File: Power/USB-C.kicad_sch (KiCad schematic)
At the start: 40 parts, among them J1 USB_C_Receptacle_PowerOnly_6P, J2 Barrel_Jack_Switch, J3 Barrel_Jack_Switch, J4 Barrel_Jack_Switch, J5 Barrel_Jack_Switch, SW1 15v12, SW2 12v9, U1 HUSB237, U2 TPS73801, U3 TPS73801

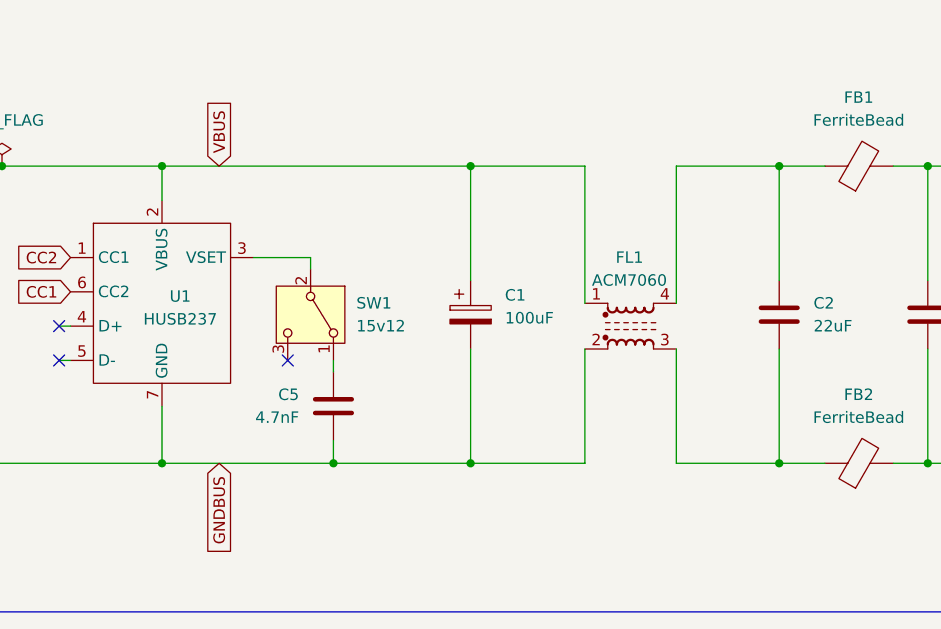
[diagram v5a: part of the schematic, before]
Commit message: Power board: move common mode choke to front
I don't do the nice 3D models, because I'm lazy and it's too much of a
hassle.  But it also means that it wasn't visually obvious that the
common mode choke ends up being very inconvenient on the back of the
board.

I'm perfectly fine with the usual low profile SMD components there, but
that choke is 3.5mm high, which is about twice as much as the other
components.

It's not that bad on the power board (which I don't have an enclosure
for anyway, although I'm looking at maybe just encasing it in resin with
a mold).  On the VGND effects board it's a non-starter.

Of course, I'm not convinced the choke actually matters, and the answer
may just be to remove it again, but until I see the effects of it let's
just move it to the front of the board.

It's going to be inconvenient to solder - I much prefer the hotplate -
but particularly on the power board I already have that USB-C connector
that I do with a hot-air station, and they are right next to each other,
so I can probably just do them together.

I'll have to think about the effects board more.  I don't actually have
room on the top of the board because I want to keep the electrolytics up
there, and keep the area in the middle clear for if I ever re-introduce
the joiner/splitter model with a third audio jack.

I think the inter-board connector there in the middle was a mistake.
It's in the way not only for this choke, but for any single-pot design
if I ever do one.

So the solution may be that I'll just have to move the connector around,
but that obviously means that I lose backwards compatibility with
existing effects boards.  Not really a big deal - unlike the enclosure
changes, it's easy enough to just do new boards - but if I make that
kind of change I want to make sure I think it through and get it right.

So let's wait to see if the choke even makes a difference.

Signed-off-by: Linus Torvalds <torvalds@linux-foundation.org>
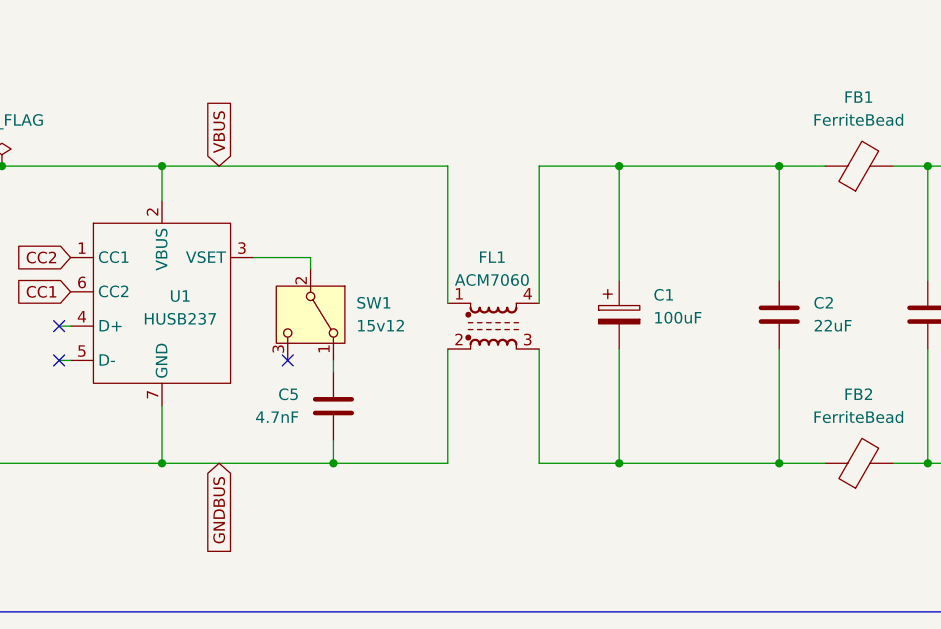
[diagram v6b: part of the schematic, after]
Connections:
- net GNDBUS: no longer C1.2
- net VBUS: no longer C1.1
- net at C2.1, FB1.1, FL1.4: now also C1.1
- net at C2.2, FB2.1, FL1.3: now also C1.2
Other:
- moved on the sheet: C1, FL1
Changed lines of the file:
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@@
 	)
 	(junction
-		(at 27.94 146.05)
+		(at 129.54 50.8)
 		(diameter 0)
 		(color 0 0 0 0)
 	)
 	(junction
-		(at 44.45 130.81)
+		(at 129.54 83.82)
 		(diameter 0)
 		(color 0 0 0 0)
 	)
 	(junction
-		(at 100.33 140.97)
+		(at 27.94 146.05)
 		(diameter 0)
 		(color 0 0 0 0)
 	)
 	(junction
-		(at 113.03 50.8)
+		(at 44.45 130.81)
 		(diameter 0)
 		(color 0 0 0 0)
 	)
 	(junction
-		(at 78.74 50.8)
+		(at 100.33 140.97)
 		(diameter 0)
 		(color 0 0 0 0)
 	)
 	(junction
-		(at 97.79 83.82)
+		(at 78.74 50.8)
 		(diameter 0)
 		(color 0 0 0 0)
 	)
 	(junction
-		(at 113.03 83.82)
+		(at 97.79 83.82)
 		(diameter 0)
 		(color 0 0 0 0)
@@
 	(wire
 		(pts
-			(xy 135.89 83.82) (xy 147.32 83.82)
+			(xy 120.65 83.82) (xy 129.54 83.82)
+		)
+		(stroke
+			(width 0)
+			(type default)
+		)
+	)
+	(wire
+		(pts
+			(xy 129.54 50.8) (xy 129.54 63.5)
 		)
 		(stroke
@@
 	(wire
 		(pts
-			(xy 135.89 50.8) (xy 147.32 50.8)
+			(xy 120.65 50.8) (xy 129.54 50.8)
 		)
 		(stroke
@@
 	(wire
 		(pts
-			(xy 113.03 50.8) (xy 113.03 63.5)
+			(xy 25.4 143.51) (xy 27.94 143.51)
 		)
 		(stroke
@@
 	(wire
 		(pts
-			(xy 25.4 143.51) (xy 27.94 143.51)
+			(xy 129.54 71.12) (xy 129.54 83.82)
 		)
 		(stroke
@@
 	(wire
 		(pts
-			(xy 113.03 83.82) (xy 125.73 83.82)
+			(xy 97.79 83.82) (xy 110.49 83.82)
 		)
 		(stroke
@@
 	(wire
 		(pts
-			(xy 135.89 71.12) (xy 135.89 83.82)
+			(xy 120.65 71.12) (xy 120.65 83.82)
 		)
 		(stroke
@@
 	(wire
 		(pts
-			(xy 113.03 71.12) (xy 113.03 83.82)
+			(xy 78.74 50.8) (xy 110.49 50.8)
 		)
 		(stroke
@@
 	(wire
 		(pts
-			(xy 113.03 50.8) (xy 125.73 50.8)
+			(xy 95.25 60.96) (xy 95.25 62.23)
 		)
 		(stroke
@@
 	(wire
 		(pts
-			(xy 95.25 60.96) (xy 95.25 62.23)
+			(xy 110.49 71.12) (xy 110.49 83.82)
 		)
 		(stroke
@@
 	(wire
 		(pts
-			(xy 125.73 71.12) (xy 125.73 83.82)
+			(xy 129.54 83.82) (xy 147.32 83.82)
 		)
 		(stroke
@@
 	(wire
 		(pts
-			(xy 78.74 50.8) (xy 113.03 50.8)
-		)
-		(stroke
-			(width 0)
-			(type default)
-		)
-	)
-	(wire
-		(pts
 			(xy 44.45 130.81) (xy 44.45 138.43)
 		)
@@
 	(wire
 		(pts
-			(xy 180.34 83.82) (xy 194.31 83.82)
+			(xy 129.54 50.8) (xy 147.32 50.8)
 		)
 		(stroke
@@
 	(wire
 		(pts
-			(xy 100.33 139.7) (xy 100.33 140.97)
+			(xy 180.34 83.82) (xy 194.31 83.82)
 		)
 		(stroke
@@
 	(wire
 		(pts
-			(xy 97.79 83.82) (xy 113.03 83.82)
+			(xy 100.33 139.7) (xy 100.33 140.97)
 		)
 		(stroke
@@
 	(wire
 		(pts
-			(xy 135.89 66.04) (xy 135.89 50.8)
+			(xy 120.65 66.04) (xy 120.65 50.8)
 		)
 		(stroke
@@
 	(wire
 		(pts
-			(xy 125.73 50.8) (xy 125.73 66.04)
+			(xy 110.49 50.8) (xy 110.49 66.04)
 		)
 		(stroke
@@
 	(symbol
 		(lib_id "Filter:Choke_CommonMode_FerriteCore_1423")
-		(at 130.81 68.58 0)
+		(at 115.57 68.58 0)
 		(unit 1)
 		(exclude_from_sim no)
@@
 		(fields_autoplaced yes)
 		(property "Reference" "FL1"
-			(at 130.683 60.96 0)
+			(at 115.443 60.96 0)
 			(effects
 				(font
@@
 		)
 		(property "Value" "ACM7060"
-			(at 130.683 63.5 0)
+			(at 115.443 63.5 0)
 			(effects
 				(font
@@
 		)
 		(property "Footprint" "Inductor_SMD:L_CommonModeChoke_TDK_ACM7060"
-			(at 130.81 74.93 0)
+			(at 115.57 74.93 0)
 			(effects
 				(font
@@
 		)
 		(property "Datasheet" "~"
-			(at 130.81 76.835 0)
+			(at 115.57 76.835 0)
 			(effects
 				(font
@@
 		)
 		(property "Description" "Generic common-mode choke, ferrite core, 1423 pin order"
-			(at 130.81 68.58 0)
+			(at 115.57 68.58 0)
 			(effects
 				(font
@@
 	(symbol
 		(lib_id "Device:C_Polarized")
-		(at 113.03 67.31 0)
+		(at 129.54 67.31 0)
 		(unit 1)
 		(exclude_from_sim no)
@@
 		(on_board yes)
 		(dnp no)
-		(fields_autoplaced yes)
 		(property "Reference" "C1"
-			(at 116.84 65.1509 0)
+			(at 133.35 65.1509 0)
 			(effects
 				(font
@@
 		)
 		(property "Value" "100uF"
-			(at 116.84 67.6909 0)
+			(at 133.35 67.6909 0)
 			(effects
 				(font
@@
 		)
 		(property "Footprint" "Capacitor_THT:CP_Radial_D8.0mm_P3.50mm"
-			(at 113.9952 71.12 0)
+			(at 130.5052 71.12 0)
 			(effects
 				(font
@@
 		)
 		(property "Datasheet" "~"
-			(at 113.03 67.31 0)
+			(at 129.54 67.31 0)
 			(effects
 				(font
@@
 		)
 		(property "Description" "Polarized capacitor"
-			(at 113.03 67.31 0)
+			(at 129.54 67.31 0)
 			(effects
 				(font
